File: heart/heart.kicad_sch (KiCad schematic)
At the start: 133 parts, among them J1 BatteryPort, J10 TYPE-C-31-M-12, J2 Leg_L, J3 Arm_L, J4 Head, J5 SWD_DBG, J6 SWD_DBG_PIN, J7 Arm_R, J8 Leg_R, J9 Cerebellum, Q1 BSC0702LS, Q2 2301, Q3 2N7002, Q4 NTMFS5C670NLT1G, Q5 NTMFS5C670NLT1G, Q6 2301, Q7 2N7002, Q8 NTMFS5C670NLT1G, Q9 NTMFS5C670NLT1G, U1 AMS1117-3.3, U2 TJA1042T, U3 TPS54231, U4 IP2368, U5 GD32C103TBUx, Y1 8M

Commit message: [New] Complete Heart board v2.0
1. There are two XT60 ports on heart board, one for power input, one for power output.
2. There is a 4pin GH 1.25 port, designed for CAN FD(1.CAN_H, 2.CAN_H, 3.CAN_L, 4.CAN_L)
3. USB Type C port is designed for PD charging.
4. Also there is a SWD port for flashing and debugging.
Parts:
- removed C2, C4, C6, C8: 100uf, Capacitor_THT:CP_Radial_D8.0mm_P3.50mm, symbol Device:C_Polarized_US
- removed D11, D12: SMF30A, Diode_SMD:D_SMB, symbol Diode:SM6T30A
- removed D2, D3, D7, D8, D9: BZT52C24, Diode_SMD:D_SOD-123F, symbol Diode:BZT52Bxx
- removed FB1: 220R, Resistor_SMD:R_0603_1608Metric, symbol Device:FerriteBead
- removed J1: BatteryPort, Rolling_Custom:AMASS_XT60PW-F, symbol Rolling_Custom:XT60PW-F
- removed J2: Leg_L, Rolling_Custom:XT30PW(2+2), symbol Rolling_Custom:XT30PW(2+2)
- removed J3: Arm_L, Rolling_Custom:XT30PW(2+2), symbol Rolling_Custom:XT30PW(2+2)
- removed J4: Head, Rolling_Custom:XT30PW(2+2), symbol Rolling_Custom:XT30PW(2+2)
- removed J6: SWD_DBG_PIN, Connector_JST:JST_GH_SM03B-GHS-TB_1x03-1MP_P1.25mm_Horizontal, symbol Connector:Conn_01x03_Female
- removed J7: Arm_R, Rolling_Custom:XT30PW(2+2), symbol Rolling_Custom:XT30PW(2+2)
- removed J8: Leg_R, Rolling_Custom:XT30PW(2+2), symbol Rolling_Custom:XT30PW(2+2)
- removed J9: Cerebellum, Rolling_Custom:XT30PW(2+2), symbol Rolling_Custom:XT30PW(2+2)
- removed R16, R17: 1k, Resistor_SMD:R_0402_1005Metric, symbol Device:R_US
- added C5, C6: 100nF, 10%, 100V, Capacitor_SMD:C_0603_1608Metric, symbol Device:C
- added D6, D7: SMF30A, Diode_SMD:D_SOD-123F, symbol Diode:SM6T30A
- added J1: BatteryPort, Connector_AMASS:AMASS_XT60-F_1x02_P7.20mm_Vertical, symbol Connector:Conn_01x02_Female
- added J2: PowerOutput, Connector_AMASS:AMASS_XT60-F_1x02_P7.20mm_Vertical, symbol Connector:Conn_01x02_Female
- added J3: CAN FD, Connector_JST:JST_GH_SM04B-GHS-TB_1x04-1MP_P1.25mm_Horizontal, symbol Connector_Generic_MountingPin:Conn_01x04_MountingPin
- added J5: SWD_DBG_Mounting, Connector_JST:JST_GH_BM03B-GHS-TBT_1x03-1MP_P1.25mm_Vertical, symbol Connector_Generic_MountingPin:Conn_01x03_MountingPin
- renumbered C12 to C10, C20 to C19, C3 to C2, C19 to C20, C7 to C3, C37 to C36, C38 to C37, C36 to C38, C40 to C39, C5 to C4, C41 to C40, C39 to C41, C44 to C43, C43 to C44, C46 to C45, C45 to C46, C10 to C7, C9 to C8, D15 to D10, D4 to D2, D5 to D3, D6 to D4, D10 to D5, D13 to D8, D14 to D9, J5 to J4, J10 to J8, L4 to L1, L1 to L2, L5 to L3, L2 to L4, L3 to L5, R18 to R16, R19 to R17, R20 to R18, R21 to R19, R22 to R20, R23 to R21, R24 to R22, R25 to R23, R26 to R24, R29 to R25, R27 to R26, R28 to R27, R30 to R28, R31 to R29, R32 to R30, U2 to U1, U1 to U2
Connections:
- net GNDA is gone; now on net GND: D1.1 (A1), D2.2 (A)
- net VREF_D is gone; now on net VREF+: C44.2, C46.2, L4.2
- net VREF_S is gone; now on net VREF-: C44.1, C46.1, R24.2
- net +24V: now also J2.2 (Pin_2)
- net +BATT: now also J1.2 (Pin_2)
- net BST1C: now also C5.2
- net BST2C: now also C6.2
- net CANFD_H: now also J3.1 (Pin_1), J3.2 (Pin_2)
- net CANFD_L: now also J3.3 (Pin_3), J3.4 (Pin_4)
- net GND: now also D6.2 (A2), D7.2 (A2), J1.1 (Pin_1), J2.1 (Pin_1), J3.MP (MountPin), J5.3 (Pin_3), J5.MP (MountPin)
- net SWCLK: now also U5.28 (PA14), J5.2 (Pin_2)
- net SWDIO: now also U5.25 (PA13), J5.1 (Pin_1)
- net BST2: now reaches U4.22 (BST2)
- net BST2: now also C6.1, D6.1 (A1)
- net BST1: now reaches U4.17 (BST1)
- net BST1: now also C5.1, D7.1 (A1)
- no-connect marks 21 -> 22
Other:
- moved on the sheet: D1, D2, J4

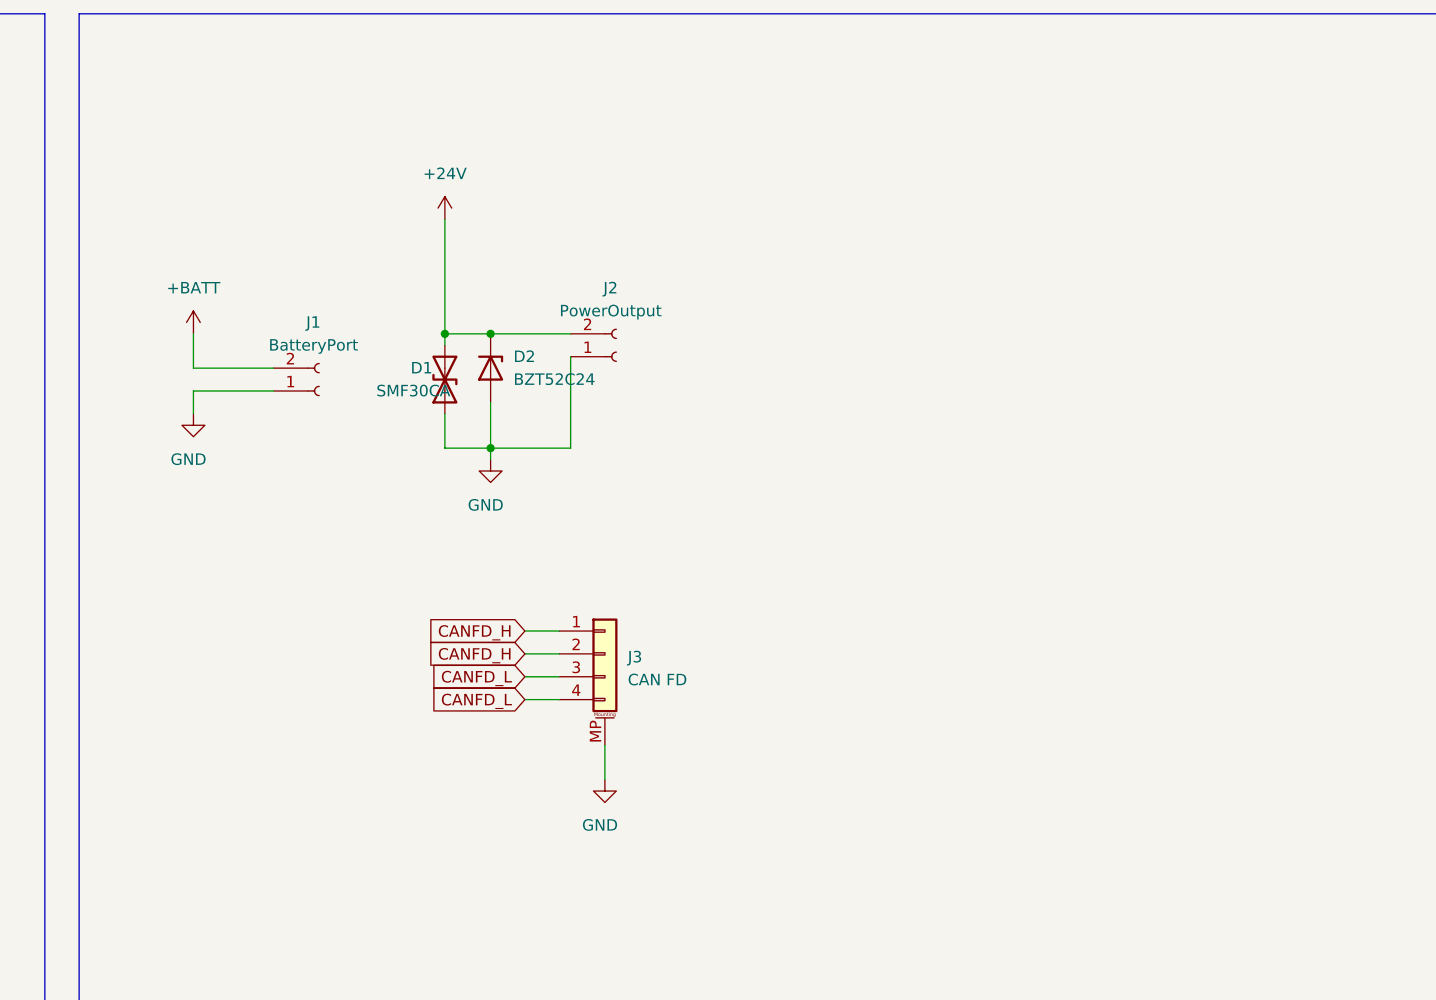
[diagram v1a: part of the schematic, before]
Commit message: [Modify] Change FP of battery power input & SWD
1. Change battery input port to XT60 M vertical.
2. Change SWD port to Horizontal.
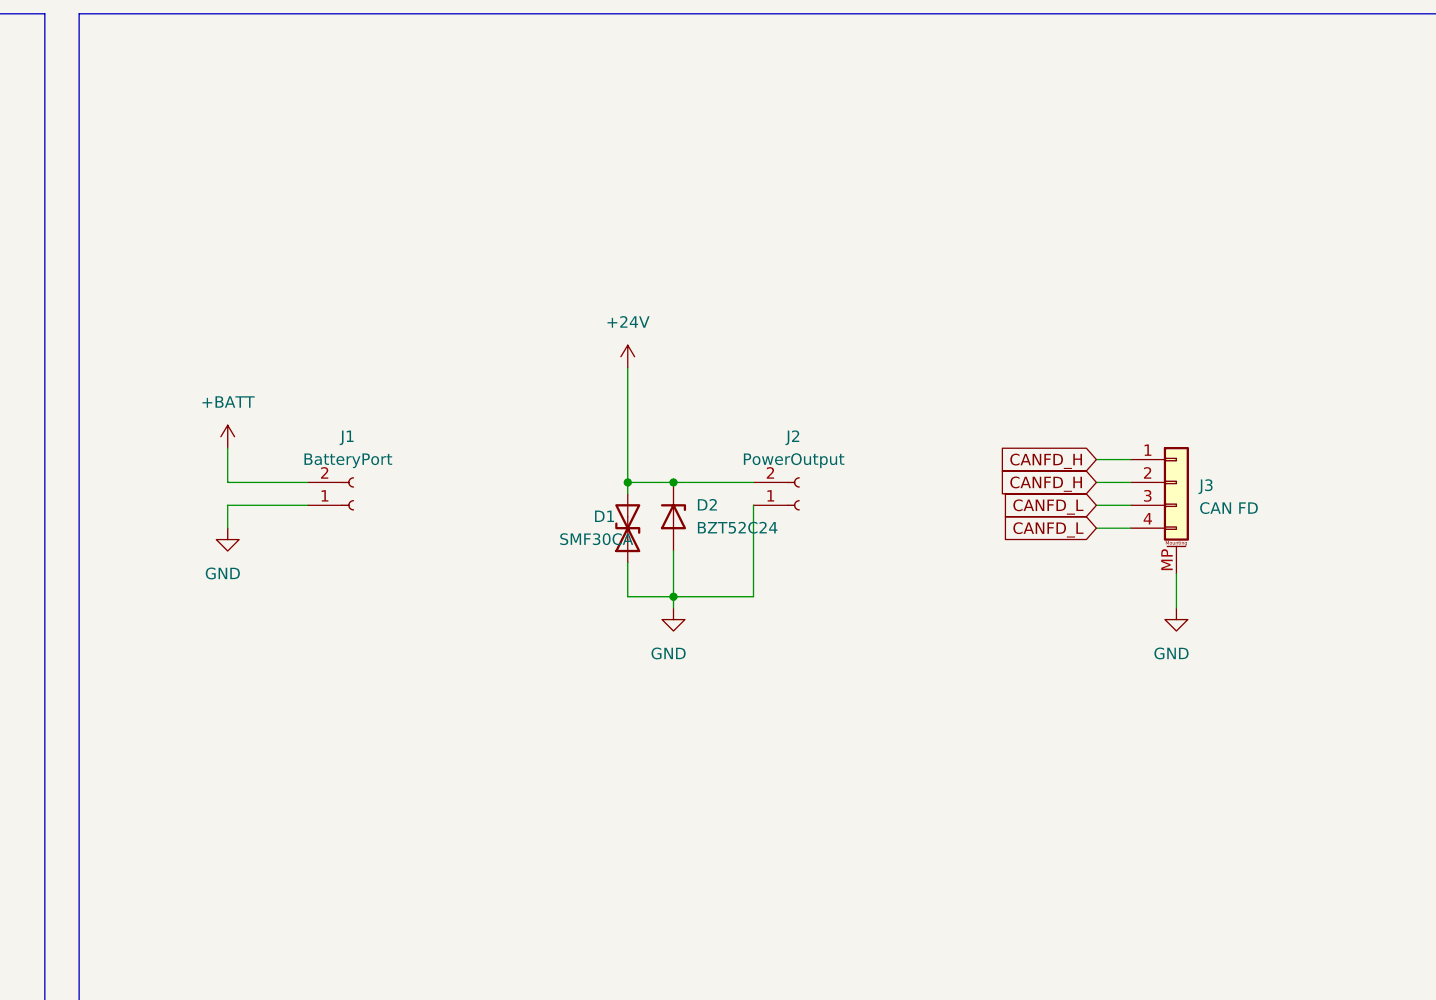
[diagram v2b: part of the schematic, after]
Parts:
- J1: footprint Connector_AMASS:AMASS_XT60-F_1x02_P7.20mm_Vertical -> Connector_AMASS:AMASS_XT60-M_1x02_P7.20mm_Vertical
- J5: footprint Connector_JST:JST_GH_BM03B-GHS-TBT_1x03-1MP_P1.25mm_Vertical -> Connector_JST:JST_GH_SM03B-GHS-TB_1x03-1MP_P1.25mm_Horizontal
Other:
- moved on the sheet: D1, D2, J1, J2, J3

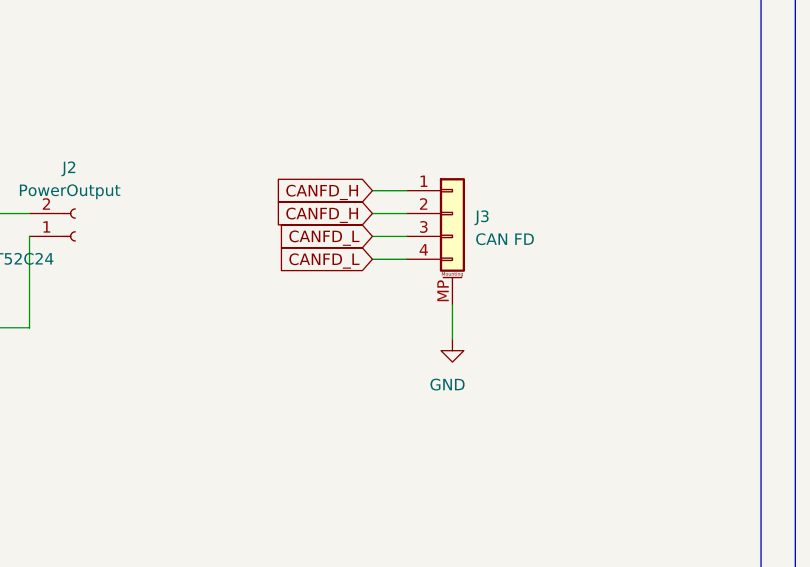
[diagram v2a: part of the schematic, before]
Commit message: [Fix] Fix XT60 layout & Change CAN ports
1. It seems 2pin is enough for  CAN FD inside the body.
2. Fix XT60 layout.
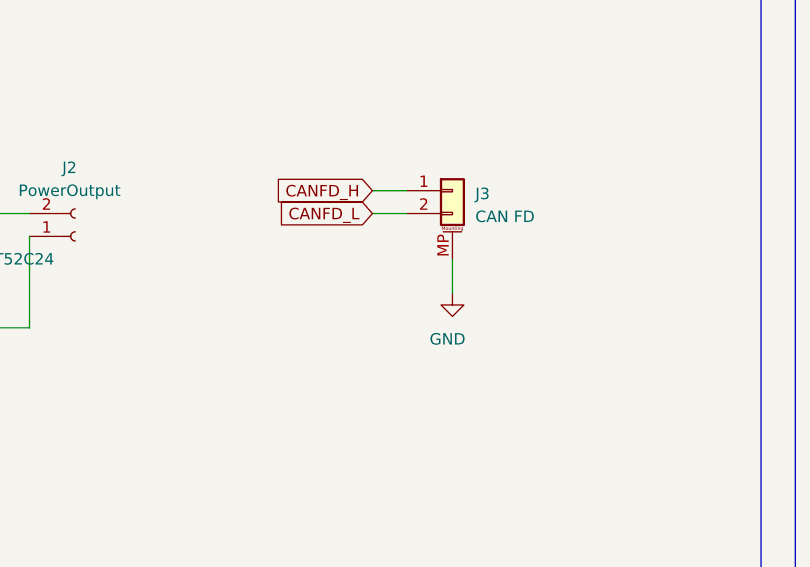
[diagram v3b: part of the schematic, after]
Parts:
- removed J3: CAN FD, Connector_JST:JST_GH_SM04B-GHS-TB_1x04-1MP_P1.25mm_Horizontal, symbol Connector_Generic_MountingPin:Conn_01x04_MountingPin
- added J3: CAN FD, Connector_JST:JST_GH_SM02B-GHS-TB_1x02-1MP_P1.25mm_Horizontal, symbol Connector_Generic_MountingPin:Conn_01x02_MountingPin
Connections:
- net CANFD_H: now also J3.1 (Pin_1)
- net CANFD_L: now also J3.2 (Pin_2)
- net GND: now also J3.MP (MountPin)
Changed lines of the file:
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@@
     (stroke (width 0) (type default) (color 0 0 0 0))
   )
-  (wire (pts (xy 175.26 80.01) (xy 175.26 83.82))
+  (wire (pts (xy 175.26 74.93) (xy 175.26 78.74))
     (stroke (width 0) (type default) (color 0 0 0 0))
   )
@@
     (stroke (width 0) (type default) (color 0 0 0 0))
   )
-  (wire (pts (xy 170.18 72.39) (xy 166.37 72.39))
+  (wire (pts (xy 170.18 69.85) (xy 166.37 69.85))
     (stroke (width 0) (type default) (color 0 0 0 0))
   )
@@
     (stroke (width 0) (type default) (color 0 0 0 0))
   )
-  (wire (pts (xy 170.18 74.93) (xy 166.37 74.93))
-    (stroke (width 0) (type default) (color 0 0 0 0))
-  )
   (wire (pts (xy 168.91 210.82) (xy 168.91 212.09))
     (stroke (width 0) (type default) (color 0 0 0 0))
@@
     (stroke (width 0) (type default) (color 0 0 0 0))
   )
-  (wire (pts (xy 170.18 69.85) (xy 166.37 69.85))
-    (stroke (width 0) (type default) (color 0 0 0 0))
-  )
   (wire (pts (xy 123.19 190.5) (xy 118.11 190.5))
     (stroke (width 0) (type default) (color 0 0 0 0))
@@
     )
   )
-  (global_label "CANFD_H" (shape input) (at 166.37 69.85 180) (fields_autoplaced)
-    (effects (font (size 1.27 1.27)) (justify right))
-    (property "Intersheet References" "${INTERSHEET_REFS}" (id 0) (at 155.7001 69.7706 0)
-      (effects (font (size 1.27 1.27)) (justify right) hide)
-    )
-  )
   (global_label "VREF-" (shape input) (at 284.48 250.19 0) (fields_autoplaced)
     (effects (font (size 1.27 1.27)) (justify left))
@@
     )
   )
-  (global_label "CANFD_L" (shape input) (at 166.37 74.93 180) (fields_autoplaced)
-    (effects (font (size 1.27 1.27)) (justify right))
-    (property "Intersheet References" "${INTERSHEET_REFS}" (id 0) (at 156.0025 74.8506 0)
-      (effects (font (size 1.27 1.27)) (justify right) hide)
-    )
-  )
   (global_label "USB_VBUS_D" (shape input) (at 311.15 62.23 0) (fields_autoplaced)
     (effects (font (size 1.27 1.27)) (justify left))
@@
     )
   )
-  (global_label "CANFD_L" (shape input) (at 166.37 72.39 180) (fields_autoplaced)
+  (global_label "CANFD_L" (shape input) (at 166.37 69.85 180) (fields_autoplaced)
     (effects (font (size 1.27 1.27)) (justify right))
-    (property "Intersheet References" "${INTERSHEET_REFS}" (id 0) (at 156.0025 72.3106 0)
+    (property "Intersheet References" "${INTERSHEET_REFS}" (id 0) (at 156.0025 69.7706 0)
       (effects (font (size 1.27 1.27)) (justify right) hide)
     )
@@
     (pin "1")
   )
+  (symbol (lib_id "Connector_Generic_MountingPin:Conn_01x02_MountingPin") (at 175.26 67.31 0) (unit 1)
+    (in_bom yes) (on_board yes) (fields_autoplaced)
+    (property "Reference" "J3" (id 0) (at 177.8 67.6655 0)
+      (effects (font (size 1.27 1.27)) (justify left))
+    )
+    (property "Value" "CAN FD" (id 1) (at 177.8 70.2055 0)
+      (effects (font (size 1.27 1.27)) (justify left))
+    )
+    (property "Footprint" "Connector_JST:JST_GH_SM02B-GHS-TB_1x02-1MP_P1.25mm_Horizontal" (id 2) (at 175.26 67.31 0)
+      (effects (font (size 1.27 1.27)) hide)
+    )
+    (property "Datasheet" "~" (id 3) (at 175.26 67.31 0)
+      (effects (font (size 1.27 1.27)) hide)
+    )
+    (pin "1")
+    (pin "2")
+    (pin "MP")
+  )
   (symbol (lib_id "power:GND") (at 300.99 161.29 0) (unit 1)
     (in_bom yes) (on_board yes)
@@
     (pin "1")
   )
-  (symbol (lib_id "power:GND") (at 175.26 83.82 0) (unit 1)
+  (symbol (lib_id "power:GND") (at 175.26 78.74 0) (unit 1)
     (in_bom yes) (on_board yes)
-    (property "Reference" "#PWR0103" (id 0) (at 175.26 90.17 0)
+    (property "Reference" "#PWR0103" (id 0) (at 175.26 85.09 0)
       (effects (font (size 1.27 1.27)) hide)
     )
-    (property "Value" "GND" (id 1) (at 172.72 88.9 0)
+    (property "Value" "GND" (id 1) (at 172.72 83.82 0)
       (effects (font (size 1.27 1.27)) (justify left))
     )
-    (property "Footprint" "" (id 2) (at 175.26 83.82 0)
+    (property "Footprint" "" (id 2) (at 175.26 78.74 0)
       (effects (font (size 1.27 1.27)) hide)
     )
-    (property "Datasheet" "" (id 3) (at 175.26 83.82 0)
+    (property "Datasheet" "" (id 3) (at 175.26 78.74 0)
       (effects (font (size 1.27 1.27)) hide)
     )
@@
     (pin "2")
   )
-  (symbol (lib_id "Connector_Generic_MountingPin:Conn_01x04_MountingPin") (at 175.26 69.85 0) (unit 1)
-    (in_bom yes) (on_board yes) (fields_autoplaced)
-    (property "Reference" "J3" (id 0) (at 177.8 70.2055 0)
-      (effects (font (size 1.27 1.27)) (justify left))
-    )
-    (property "Value" "CAN FD" (id 1) (at 177.8 72.7455 0)
-      (effects (font (size 1.27 1.27)) (justify left))
-    )
-    (property "Footprint" "Connector_JST:JST_GH_SM04B-GHS-TB_1x04-1MP_P1.25mm_Horizontal" (id 2) (at 175.26 69.85 0)
-      (effects (font (size 1.27 1.27)) hide)
-    )
-    (property "Datasheet" "~" (id 3) (at 175.26 69.85 0)
-      (effects (font (size 1.27 1.27)) hide)
-    )
-    (pin "1")
-    (pin "2")
-    (pin "3")
-    (pin "4")
-    (pin "MP")
-  )
   (symbol (lib_id "Device:C") (at 387.35 81.28 90) (mirror x) (unit 1)
     (in_bom yes) (on_board yes)
@@
       (reference "J2") (unit 1) (value "PowerOutput") (footprint "Connector_AMASS:AMASS_XT60-F_1x02_P7.20mm_Vertical")
     )
-    (path "/fd3249d5-3ada-4f2d-9834-febc614eef14"
-      (reference "J3") (unit 1) (value "CAN FD") (footprint "Connector_JST:JST_GH_SM04B-GHS-TB_1x04-1MP_P1.25mm_Horizontal")
+    (path "/a0c79021-e688-46a6-908d-4dc184524a5f"
+      (reference "J3") (unit 1) (value "CAN FD") (footprint "Connector_JST:JST_GH_SM02B-GHS-TB_1x02-1MP_P1.25mm_Horizontal")
     )
     (path "/2ee2765f-948b-4c70-b617-4c8fddc1a28e"

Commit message: [Modify] Complete descriptions in schematics
including cerebellum and heart.
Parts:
- C1: value 10pf 50V -> 10pf/50V/0402
- C10, C7: value 4.7uF 50V -> 4.7uF/50V/0805
- C11, C28, C36, C37, C39, C4, C40, C42, C50: value 100nF, 10%, 50V -> 100nF/50V/0402
- C13: value 22uF, 10%, 6.3V -> 22uF/6.3V/0402
- C14, C2, C30, C8: value 10uf 50V -> 10uf/50V/0402
- C15: value 8.2nf 50V -> 8.2nf/50V/0603
- C16, C17: value 100pF, 10%, 10V -> 100pF/50V/0402
- C18, C20, C22, C24, C29, C41, C46: value 100nF, 10%, 10V -> 100nF/10V/0402
- C19, C21: value 47uf 50V -> 47uf/50V/0603
- C23, C26: value 20pF, 10%, 10V -> 20pF/10V/0402
- C25: value 4.7uF, 10%, 10V -> 4.7uF/10V/0402
- C27: value 1uF, 10%, 10V -> 1uF/10V/0402
- C3: value 1.5nf 50V -> 1.5nf/50V/0603
- C31, C33: value 1uf 50V -> 1uf/50V/0603
- C32, C34, C35: value 2.2uf 50v -> 2.2uf/50v/0201
- C38, C44: value 10uF, 10%, 10V -> 10uF/10V/0402
- C43, C49: value 220uf -> 220uf/50V
- C45, C47, C48, C51, C54, C55: value 22uF,50V -> 22uF/50V/2220
- C5, C6: value 100nF, 10%, 100V -> 100nF/100V/0603
- C52, C53: value 1.5nF 50v -> 1.5nF/50v/0402
- L2: value 15uh, SLO0530H150MTT -> 15uh/SLO0530H150MTT
- R1: value 64.9k -> 64.9k/0402
- R10, R11: value 4.7k -> 4.7k/0402
- R12, R15: value 27k -> 27k/0402
- R13: value 6.2k -> 6.2k/0402
- R14, R22, R25: value 10k -> 10k/0402
- R16, R17, R24: value 0 -> 0R/0402
- R18, R20: value 10r -> 10R/0402
- R19, R21: value 0.005r -> 0.005R/0805
- R2: value 169k -> 169k/0402
- R23, R28: value 1M -> 1M/0402
- R26, R27: value 330r -> 330R/0402
- R29, R30: value 2r -> 2R/0402
- R3: value 20.5 -> 20.5/0402
- R4: value 120R -> 120R/0402
- R5, R8: value 10k, 5% -> 10k/5%/0402
- R6: value 10.2k -> 10.2k/0402
- R7: value 1.96k -> 1.96k/0402
- R9: value 10k, 3380k -> 10k/3380k/0402

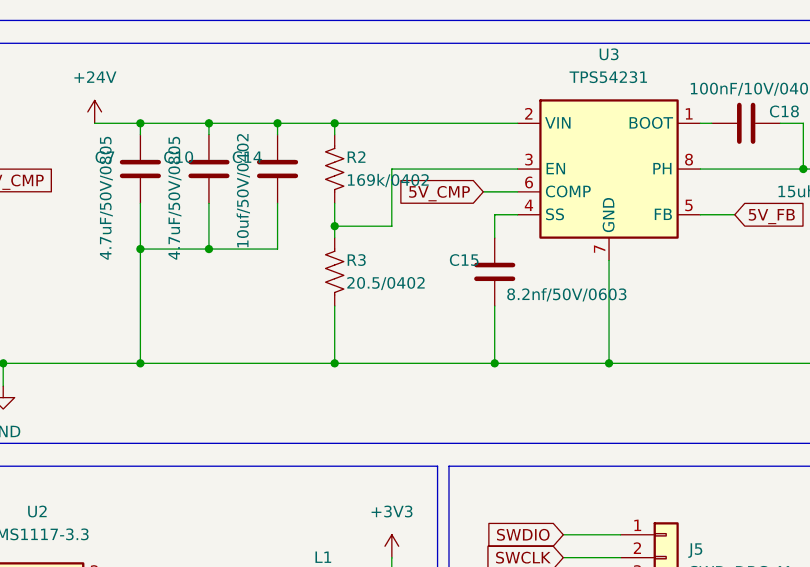
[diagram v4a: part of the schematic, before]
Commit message: [Fix] Complete resistor value of 24Vto5V regulator
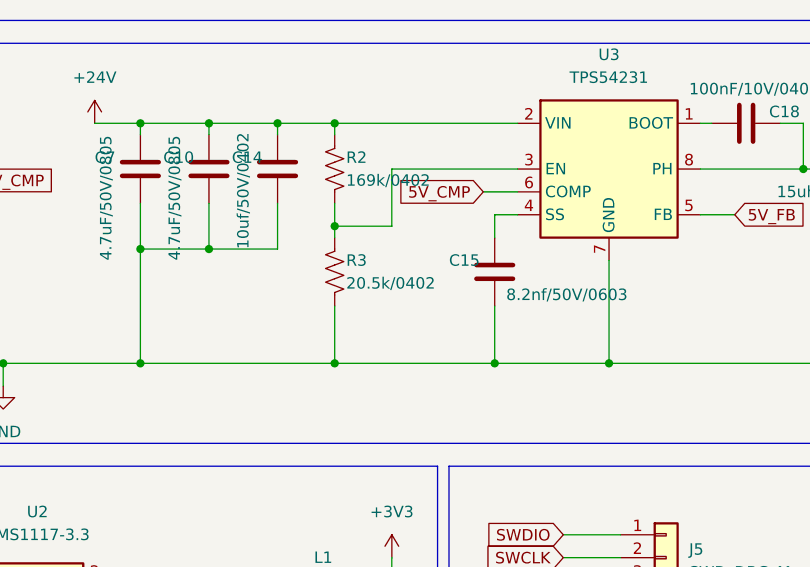
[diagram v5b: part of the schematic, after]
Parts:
- R3: value 20.5/0402 -> 20.5k/0402
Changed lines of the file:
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@@
       (effects (font (size 1.27 1.27)) (justify right))
     )
-    (property "Value" "20.5/0402" (id 1) (at 92.71 157.48 0)
+    (property "Value" "20.5k/0402" (id 1) (at 92.71 157.48 0)
       (effects (font (size 1.27 1.27)) (justify right))
     )
@@
     )
     (path "/7a86fa65-d6c6-4ad2-87df-110da7c744e1"
-      (reference "R3") (unit 1) (value "20.5/0402") (footprint "Resistor_SMD:R_0402_1005Metric")
+      (reference "R3") (unit 1) (value "20.5k/0402") (footprint "Resistor_SMD:R_0402_1005Metric")
     )
     (path "/f72c6069-4960-4124-8d65-281cb3212cc9"
